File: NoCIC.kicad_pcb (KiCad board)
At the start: 2 copper layers, 9.5 x 20.6 mm, 12 parts, among them J1 CIC, U1 74LVC1G06, U2 LMC555xM, U3 74LVC1G04

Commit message: Add basic README
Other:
- board text added: "NoCIC"
- board text added: "Rev. 1"
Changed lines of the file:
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@@
 		(tags "capacitor handsolder")
 		(property "Reference" "C4"
-			(at 2.159 0 90)
+			(at -2.159 0 90)
 			(layer "F.SilkS")
 			(effects
@@
 		(tags "resistor handsolder")
 		(property "Reference" "R1"
-			(at -2.443 1.143 90)
+			(at -2.443 1.143 180)
 			(layer "B.SilkS")
 			(effects
@@
 		(tags "capacitor handsolder")
 		(property "Reference" "C1"
-			(at -2.413 0.508 90)
+			(at -2.413 0.508 180)
 			(layer "B.SilkS")
 			(effects
@@
 		(tags "resistor handsolder")
 		(property "Reference" "R3"
-			(at -2.397 0 90)
+			(at -2.397 0 180)
 			(layer "B.SilkS")
 			(effects
@@
 		(tags "capacitor handsolder")
 		(property "Reference" "C2"
-			(at -2.413 0 90)
+			(at -2.413 0 180)
 			(layer "B.SilkS")
 			(effects
@@
 		(tags "capacitor handsolder")
 		(property "Reference" "C3"
-			(at -2.413 0 90)
+			(at -2.413 0 180)
 			(layer "B.SilkS")
 			(effects
@@
 		)
 	)
+	(gr_circle
+		(center 107.569 69.85)
+		(end 107.696 70.104)
+		(stroke
+			(width 0.1)
+			(type default)
+		)
+		(fill no)
+		(layer "F.SilkS")
+	)
 	(gr_line
 		(start 114.427 69.207)
@@
 		(layer "Edge.Cuts")
 	)
+	(gr_text "NoCIC"
+		(at 109.652 89.1 0)
+		(layer "F.SilkS")
+		(effects
+			(font
+				(size 0.7 1)
+				(thickness 0.1)
+			)
+			(justify bottom)
+		)
+	)
+	(gr_text "Rev. 1"
+		(at 109.601 70.104 0)
+		(layer "B.SilkS")
+		(effects
+			(font
+				(size 0.6 0.6)
+				(thickness 0.1)
+			)
+			(justify mirror)
+		)
+	)
 	(segment

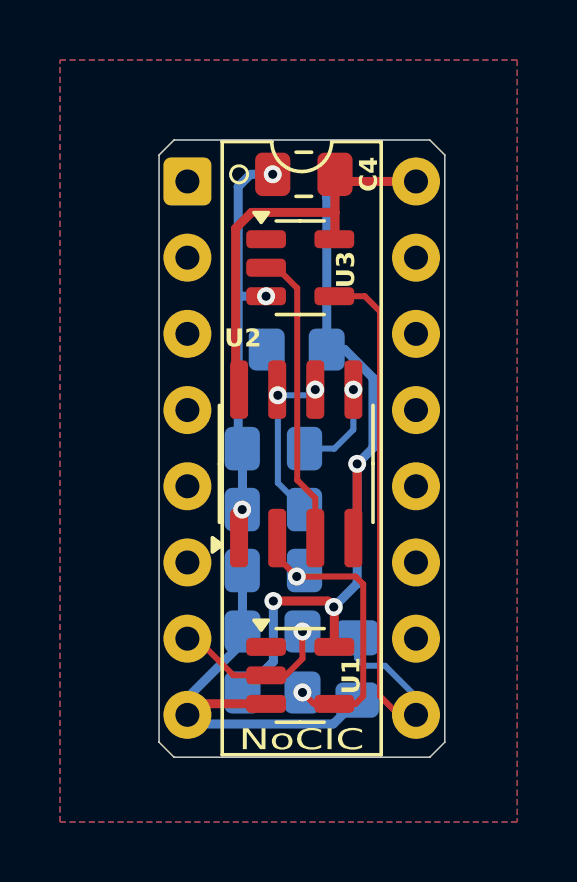
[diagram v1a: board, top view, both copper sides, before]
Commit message: Add a jumper option to connect 555 output to pin 10, for CIC-RESET
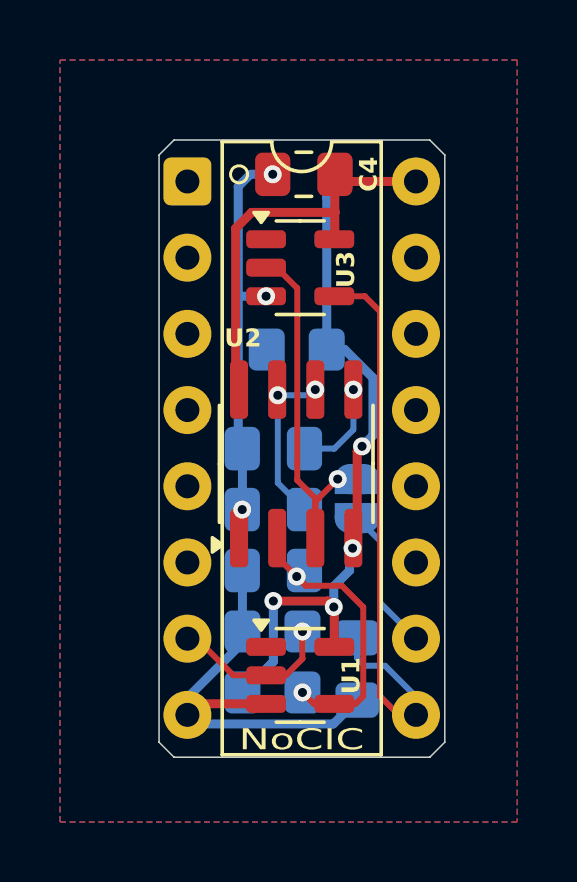
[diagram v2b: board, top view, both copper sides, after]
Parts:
- added JP1: CIC-RESET Enabled, Jumper:SolderJumper-2_P1.3mm_Open_RoundedPad1.0x1.5mm, B.Cu at (111.5, 80.7)
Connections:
- J1 pad 10: unconnected-(J1-Pin_10-Pad10) -> /CIC-RST
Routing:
- net /CIC-RST: track 0.00 -> 4.83 mm
- net VCC: track 41.7 -> 38.9 mm, vias 3 -> 4
- net Net-(JP1-A): track 9.90 -> 12.3 mm, vias 0 -> 1
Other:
- board text added: "Rev. 2"
- board text removed: "Rev. 1"

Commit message: Add load resistors on data lines
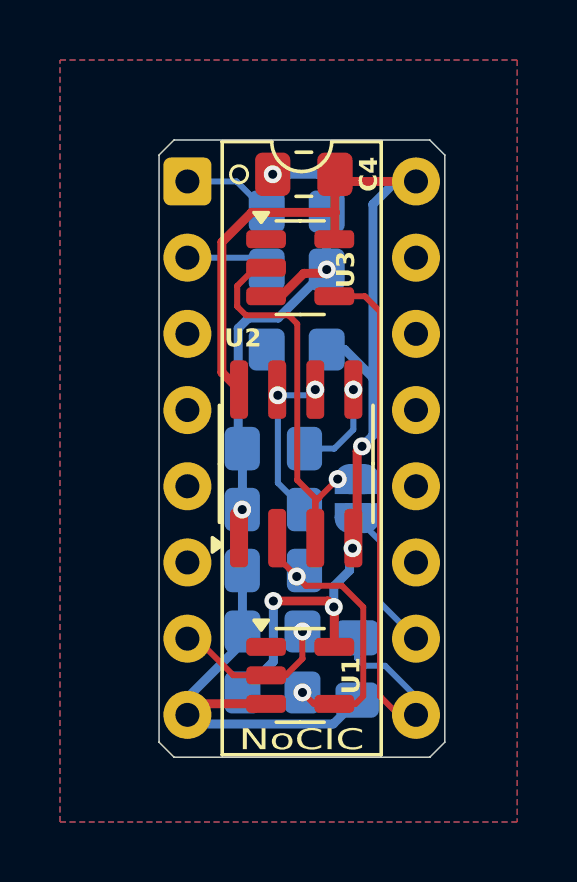
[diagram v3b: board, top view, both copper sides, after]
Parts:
- added R4: 1K, Resistor_SMD:R_0805_2012Metric_Pad1.20x1.40mm_HandSolder, B.Cu at (109.5, 71.1)
- added R5: 1K, Resistor_SMD:R_0805_2012Metric_Pad1.20x1.40mm_HandSolder, B.Cu at (109.5, 73.0)
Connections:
- J1 pad 1: unconnected-(J1-Pin_1-Pad1) -> Net-(J1-Pin_1)
- J1 pad 2: unconnected-(J1-Pin_2-Pad2) -> Net-(J1-Pin_2)
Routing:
- net GND: track 30.6 -> 34.7 mm
- net Net-(J1-Pin_1): track 0.00 -> 3.06 mm
- net Net-(J1-Pin_2): track 0.00 -> 2.81 mm
- net Net-(JP1-A): track 12.3 -> 13.9 mm
